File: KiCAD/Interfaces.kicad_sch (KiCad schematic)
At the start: 56 parts, among them X2 Keyboard + User IO, X3 Centronics, X4 FDD-Connector, X5 User IO

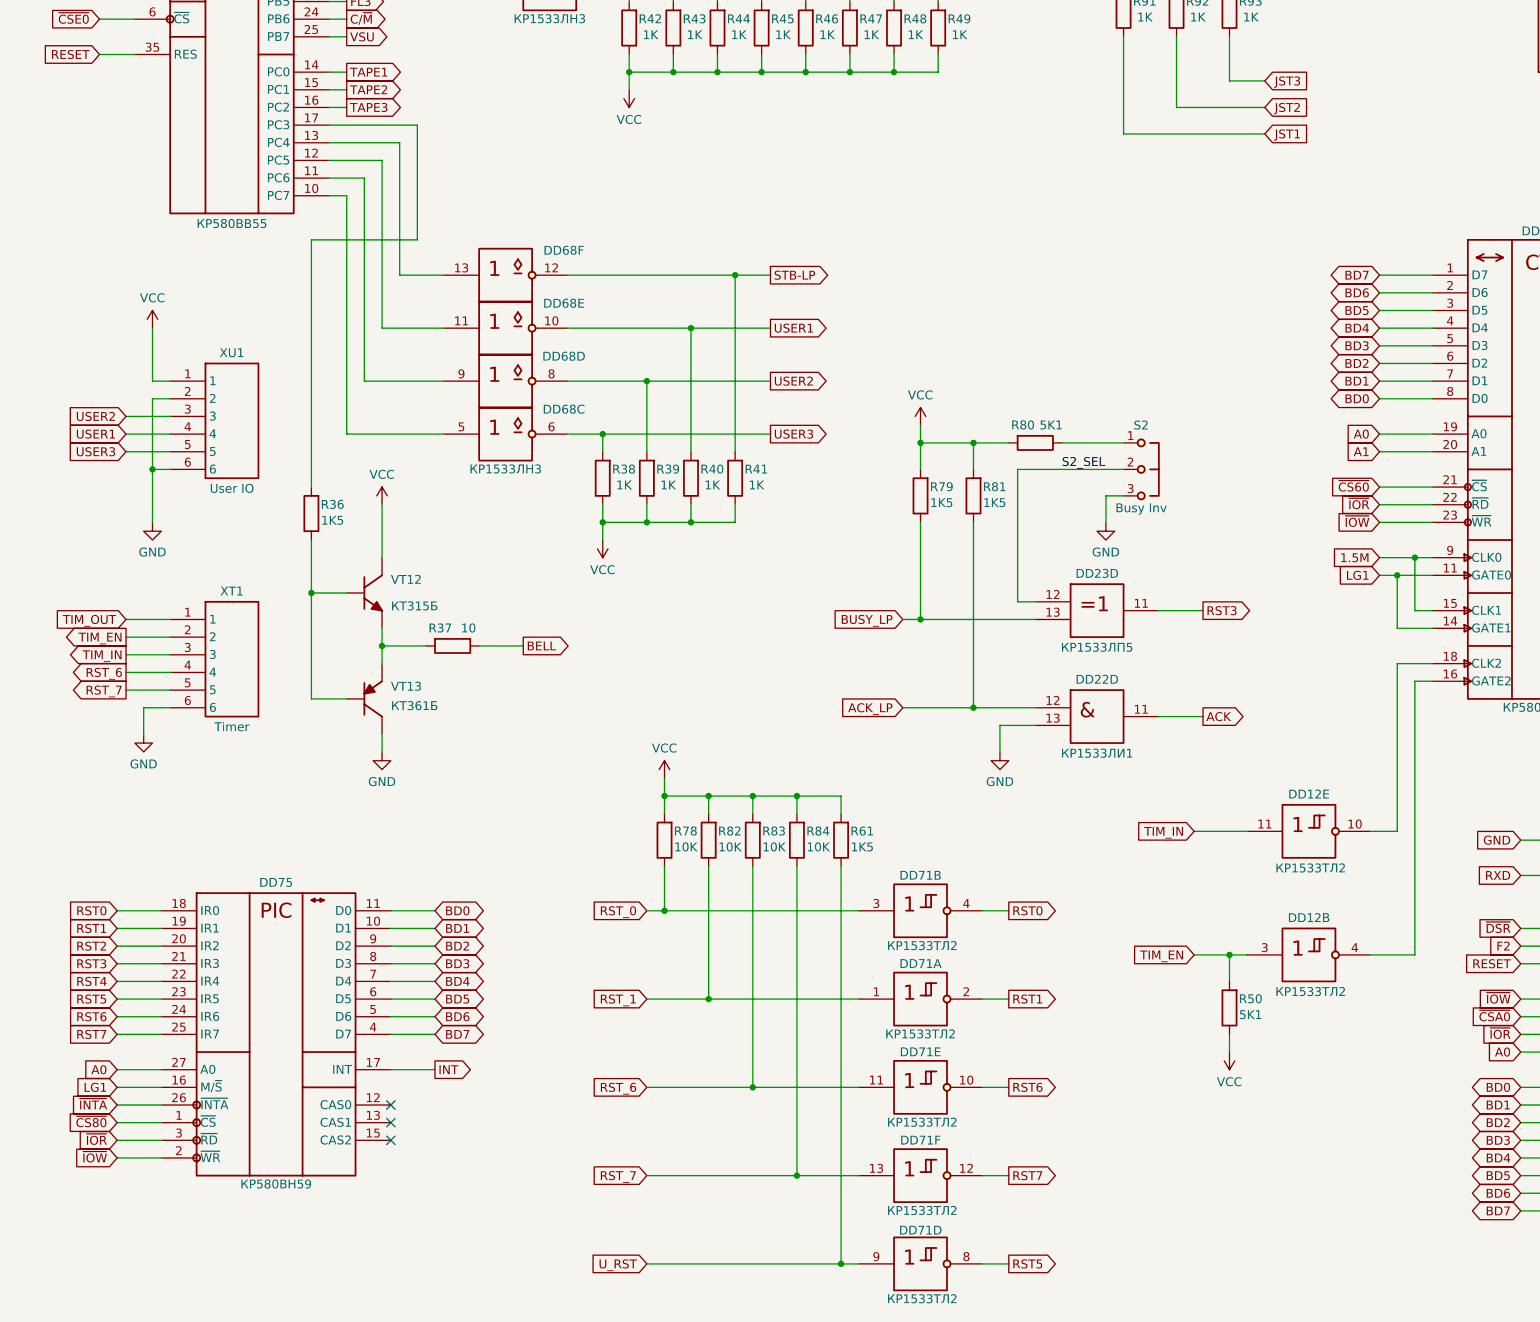
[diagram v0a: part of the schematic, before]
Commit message: Fix DD5 and DD22
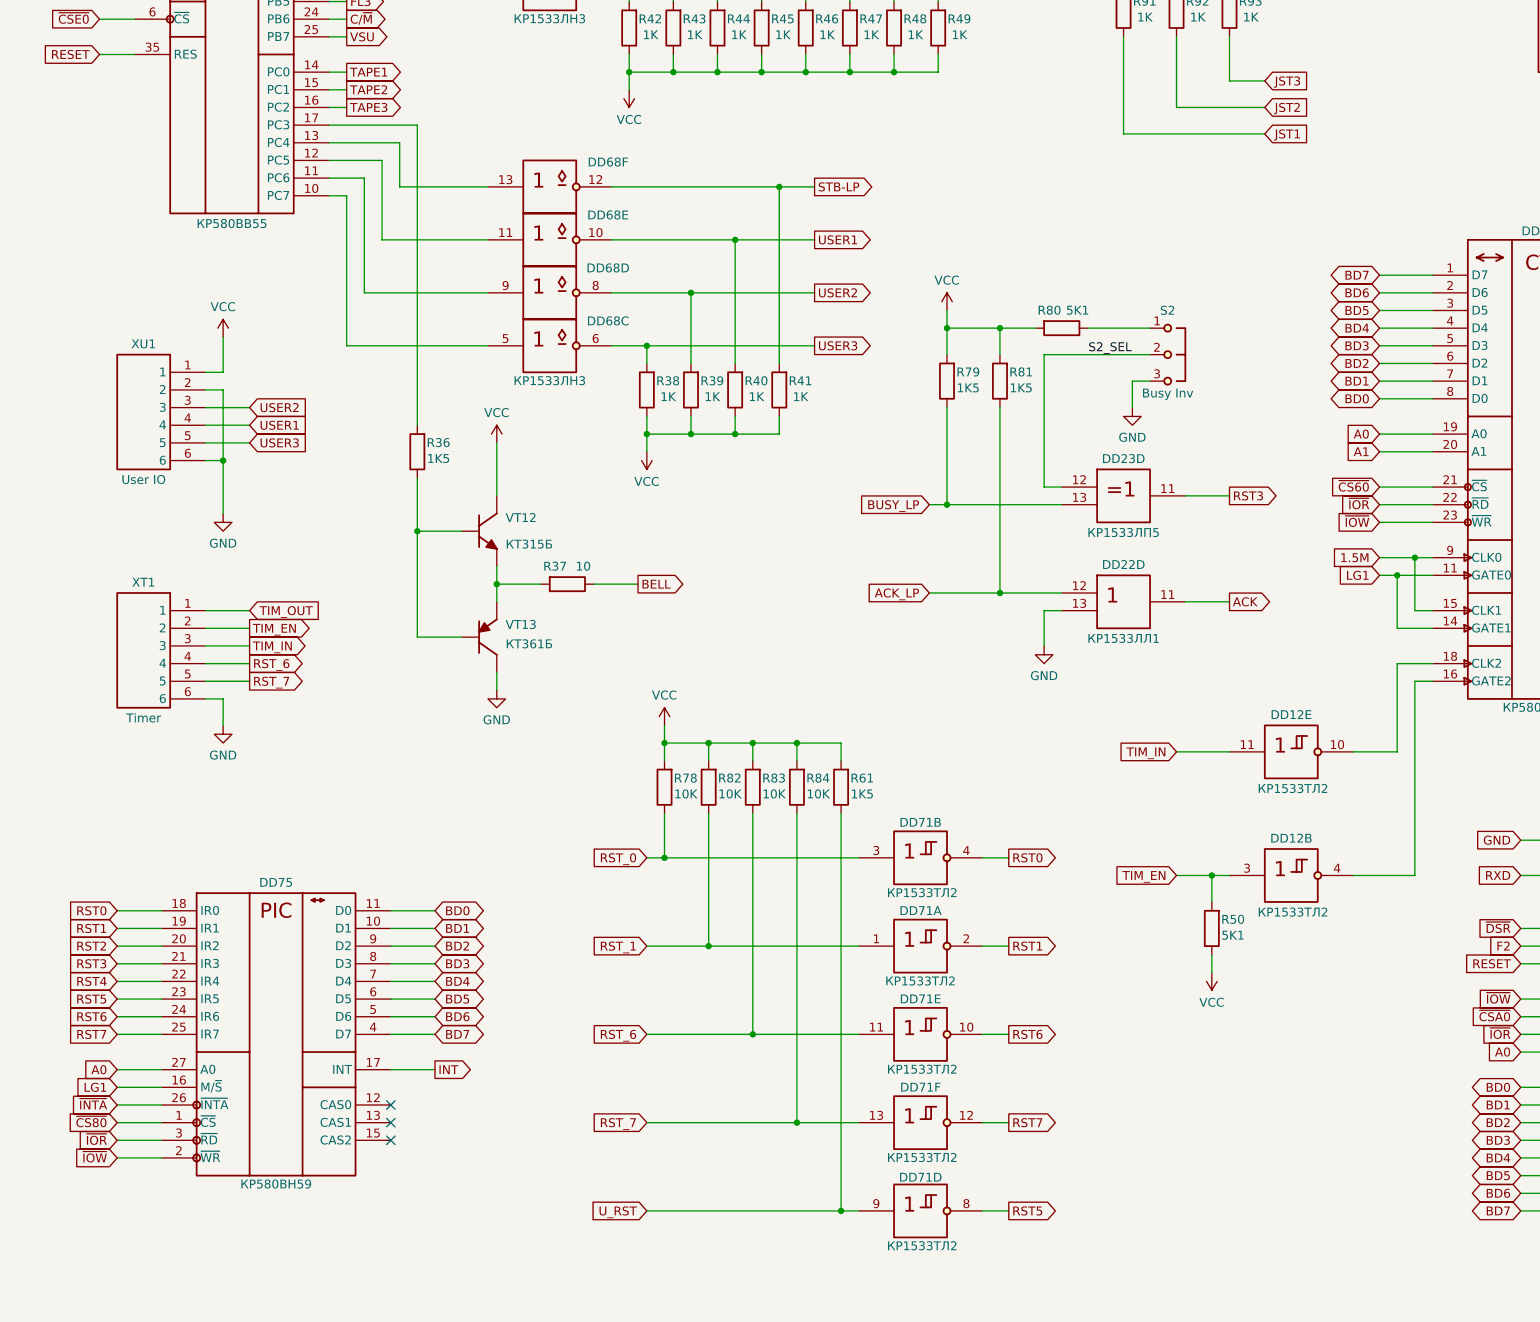
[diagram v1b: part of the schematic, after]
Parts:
- removed DD22: КР1533ЛИ1, Romychs_IC_DIP:DIP-14_W7.62mm, symbol Romychs_Logic_TTL:КР1533ЛИ1
- added DD22: КР1533ЛЛ1, Romychs_IC_DIP:DIP-14_W7.62mm, symbol Romychs_Logic_TTL:КР1533ЛЛ1
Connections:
- net ACK: now also DD22.11 (3)
- net ACK_LP: now also DD22.12 (1)
- net GND: now also DD22.13 (2)
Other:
- moved on the sheet: DD12B, DD12E, DD23D, DD68C, DD68D, DD68E, DD68F, DD71A, DD71B, DD71D, DD71E, DD71F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
